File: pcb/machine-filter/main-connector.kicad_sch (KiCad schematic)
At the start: 3 parts

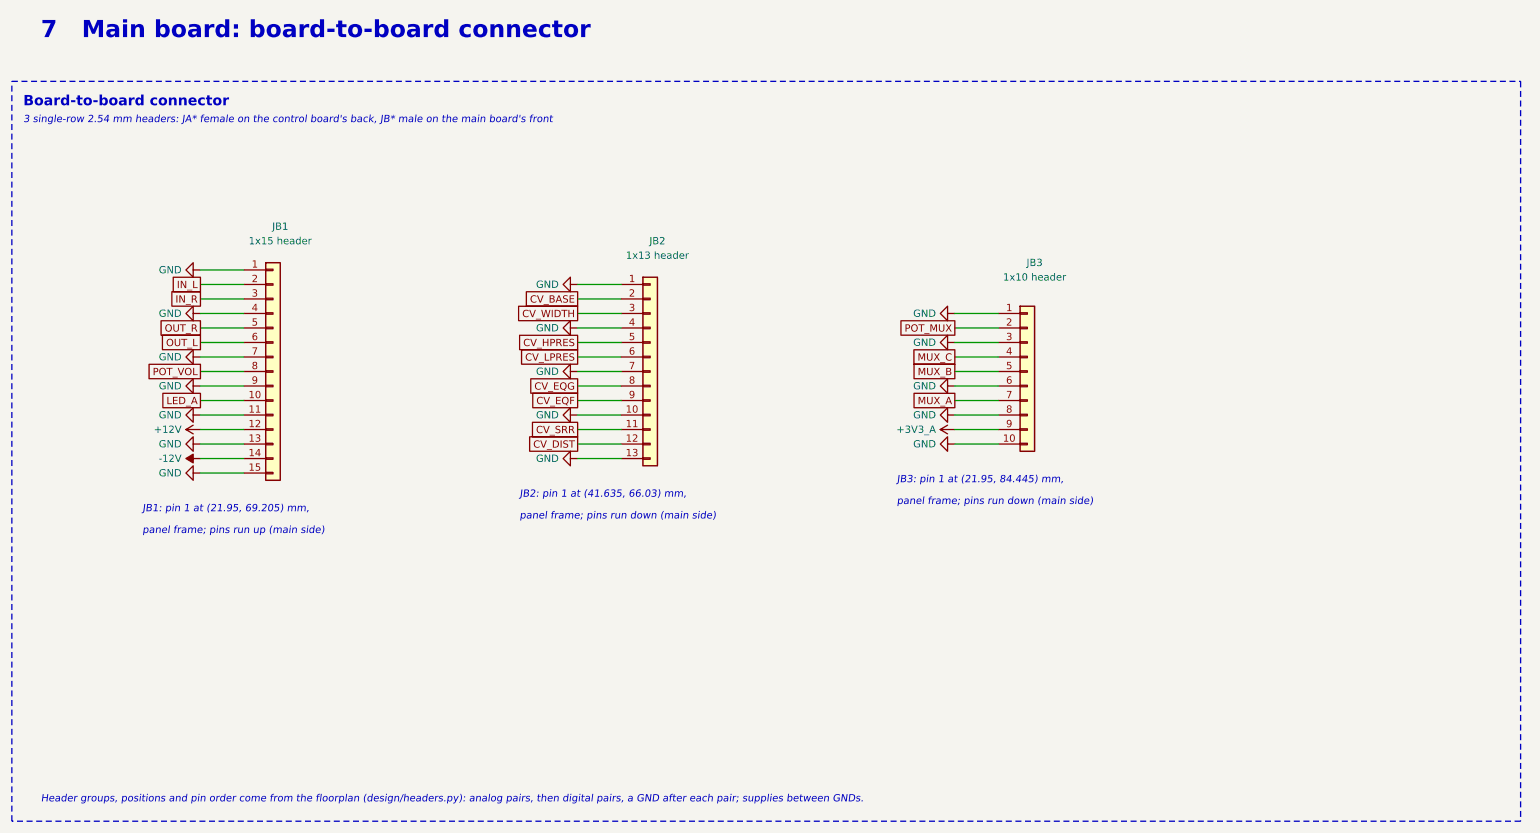
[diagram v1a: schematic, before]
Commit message: Control chips placed; board-to-board connectors found by search: 4 lines (22+3+5+3 pins, 12 ground)
connector_search.py: lines live in legal straight runs on both boards (courtyard polygons, socket body and its
courtyard, leads under bodies), d's ground rules plus a ground on every connector; simulated annealing, 12
restarts. sync_headers.py deletes and re-adds the header footprints from the schematic, places both boards and
checks every pin pair lines up. auto_place.py now keeps other parts' leads out from under a body (U6 had RV4's
lead under it). Mux channels and LED sections re-checked: already shortest. Build OK, raw DRC: no real problems.

Co-Authored-By: Claude Opus 5.5 <noreply@anthropic.com>
Claude-Session: https://claude.ai/code/session_01Cf5qNBi3oNHhbCjPHvswth
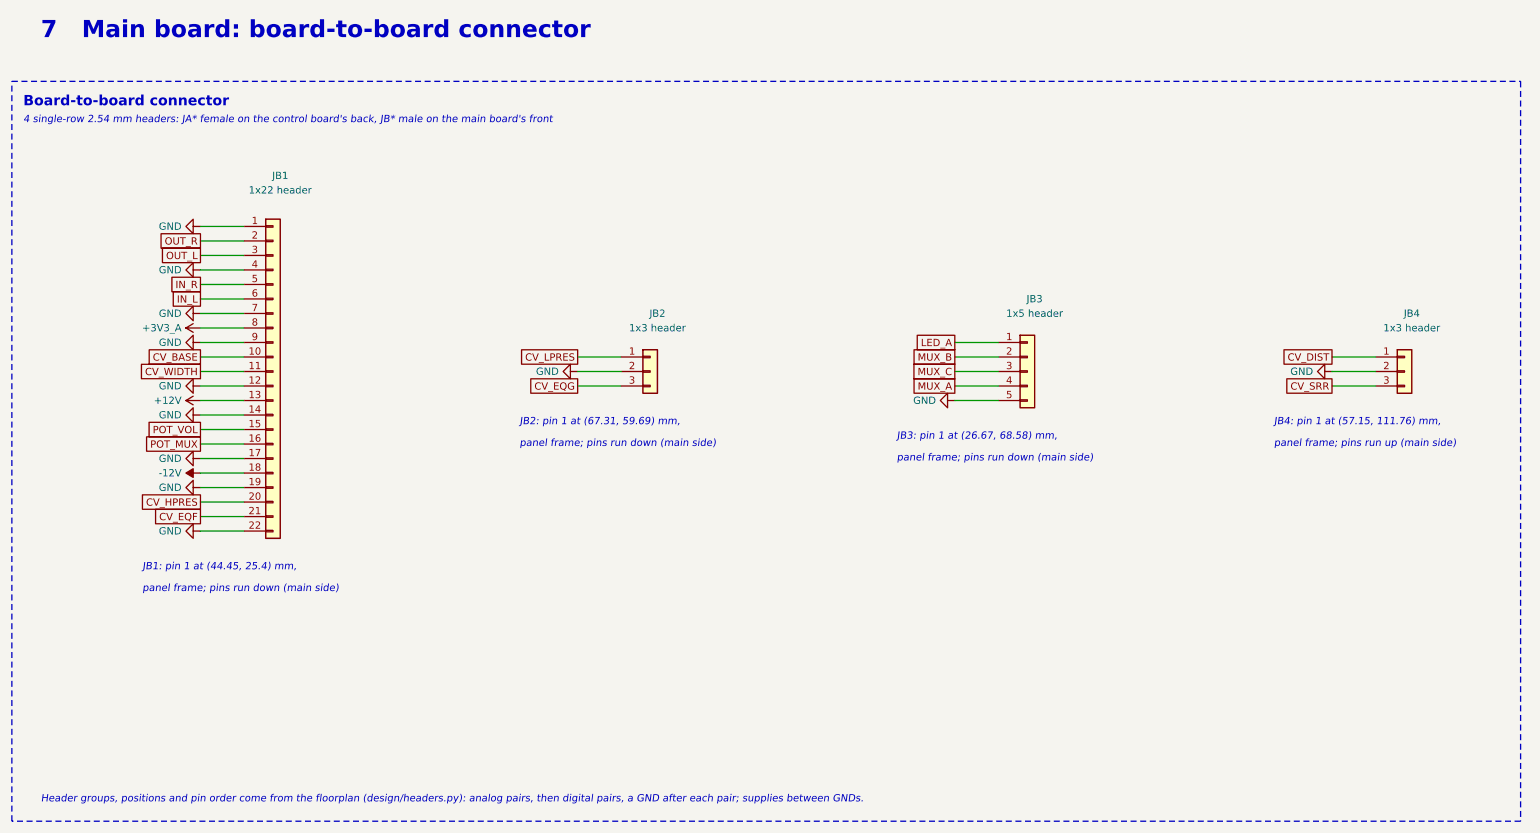
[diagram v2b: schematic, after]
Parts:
- added JB4: 1x3 header, Connector_PinHeader_2.54mm:PinHeader_1x03_P2.54mm_Vertical, symbol Connector_Generic:Conn_01x03
- JB1: value 1x15 header -> 1x22 header; footprint Connector_PinHeader_2.54mm:PinHeader_1x15_P2.54mm_Vertical -> Connector_PinHeader_2.54mm:PinHeader_1x22_P2.54mm_Vertical; symbol Connector_Generic:Conn_01x15 -> Connector_Generic:Conn_01x22; MPN 2.54 mm male pin header 1x15 -> 2.54 mm male pin header 1x22
- JB2: value 1x13 header -> 1x3 header; footprint Connector_PinHeader_2.54mm:PinHeader_1x13_P2.54mm_Vertical -> Connector_PinHeader_2.54mm:PinHeader_1x03_P2.54mm_Vertical; symbol Connector_Generic:Conn_01x13 -> Connector_Generic:Conn_01x03; MPN 2.54 mm male pin header 1x13 -> 2.54 mm male pin header 1x3
- JB3: value 1x10 header -> 1x5 header; footprint Connector_PinHeader_2.54mm:PinHeader_1x10_P2.54mm_Vertical -> Connector_PinHeader_2.54mm:PinHeader_1x05_P2.54mm_Vertical; symbol Connector_Generic:Conn_01x10 -> Connector_Generic:Conn_01x05; MPN 2.54 mm male pin header 1x10 -> 2.54 mm male pin header 1x5
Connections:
- net +12V: now also JB1.13 (Pin_13); no longer JB1.12 (Pin_12)
- net +3V3_A: now also JB1.8 (Pin_8); no longer JB3.9 (Pin_9)
- net -12V: now also JB1.18 (Pin_18); no longer JB1.14 (Pin_14)
- net CV_BASE: now also JB1.10 (Pin_10); no longer JB2.2 (Pin_2)
- net CV_DIST: now also JB4.1 (Pin_1); no longer JB2.12 (Pin_12)
- net CV_EQF: now also JB1.21 (Pin_21); no longer JB2.9 (Pin_9)
- net CV_EQG: now also JB2.3 (Pin_3); no longer JB2.8 (Pin_8)
- net CV_HPRES: now also JB1.20 (Pin_20); no longer JB2.5 (Pin_5)
- net CV_LPRES: now also JB2.1 (Pin_1); no longer JB2.6 (Pin_6)
- net CV_SRR: now also JB4.3 (Pin_3); no longer JB2.11 (Pin_11)
- net CV_WIDTH: now also JB1.11 (Pin_11); no longer JB2.3 (Pin_3)
- net GND: now also JB1.12 (Pin_12), JB1.14 (Pin_14), JB1.17 (Pin_17), JB1.19 (Pin_19), JB1.22 (Pin_22), JB2.2 (Pin_2), JB3.5 (Pin_5), JB4.2 (Pin_2); no longer JB1.11 (Pin_11), JB1.13 (Pin_13), JB1.15 (Pin_15), JB2.1 (Pin_1), JB2.10 (Pin_10), JB2.13 (Pin_13), JB2.4 (Pin_4), JB2.7 (Pin_7), JB3.1 (Pin_1), JB3.10 (Pin_10), JB3.3 (Pin_3), JB3.6 (Pin_6), JB3.8 (Pin_8)
- net IN_L: now also JB1.6 (Pin_6); no longer JB1.2 (Pin_2)
- net IN_R: now also JB1.5 (Pin_5); no longer JB1.3 (Pin_3)
- net LED_A: now also JB3.1 (Pin_1); no longer JB1.10 (Pin_10)
- net MUX_A: now also JB3.4 (Pin_4); no longer JB3.7 (Pin_7)
- net MUX_B: now also JB3.2 (Pin_2); no longer JB3.5 (Pin_5)
- net MUX_C: now also JB3.3 (Pin_3); no longer JB3.4 (Pin_4)
- net OUT_L: now also JB1.3 (Pin_3); no longer JB1.6 (Pin_6)
- net OUT_R: now also JB1.2 (Pin_2); no longer JB1.5 (Pin_5)
- net POT_MUX: now also JB1.16 (Pin_16); no longer JB3.2 (Pin_2)
- net POT_VOL: now also JB1.15 (Pin_15); no longer JB1.8 (Pin_8)
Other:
- note added: "4 single-row 2.54 mm headers: JA* female on the control board's back, JB* male on the main board's front"
- note added: "JB1: pin 1 at (44.45, 25.4) mm,"
- note added: "JB2: pin 1 at (67.31, 59.69) mm,"
- note added: "JB3: pin 1 at (26.67, 68.58) mm,"
- note added: "JB4: pin 1 at (57.15, 111.76) mm,"
- note removed: "3 single-row 2.54 mm headers: JA* female on the control board's back, JB* male on the main board's front"
- note removed: "JB1: pin 1 at (21.95, 69.205) mm,"
- note removed: "JB2: pin 1 at (41.635, 66.03) mm,"
- note removed: "JB3: pin 1 at (21.95, 84.445) mm,"

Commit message: Hand-soldering clearance (d: 1.25 mm): connectors re-searched, control parts re-placed
connector_search.py: header pads keep 1.25 mm from every other pad on both boards and from the whole box around
each jack, pot and LED (taken from the square pin-1 pad); --free leaves parts to be re-placed out of the search.
auto_place.py: control-board through-hole pads and anything near a header keep 1.25 mm; --free re-places parts.
Result: 3 lines, 30 + 5 + 2 pins (16 ground); the connector beside pot RV5 and the one between two CV jacks are
gone. Measured: nearest header-pad gap 1.35 mm, header to a body box 1.31 mm. Raw DRC: no real problems.

Co-Authored-By: Claude Opus 5.5 <noreply@anthropic.com>
Claude-Session: https://claude.ai/code/session_01Cf5qNBi3oNHhbCjPHvswth
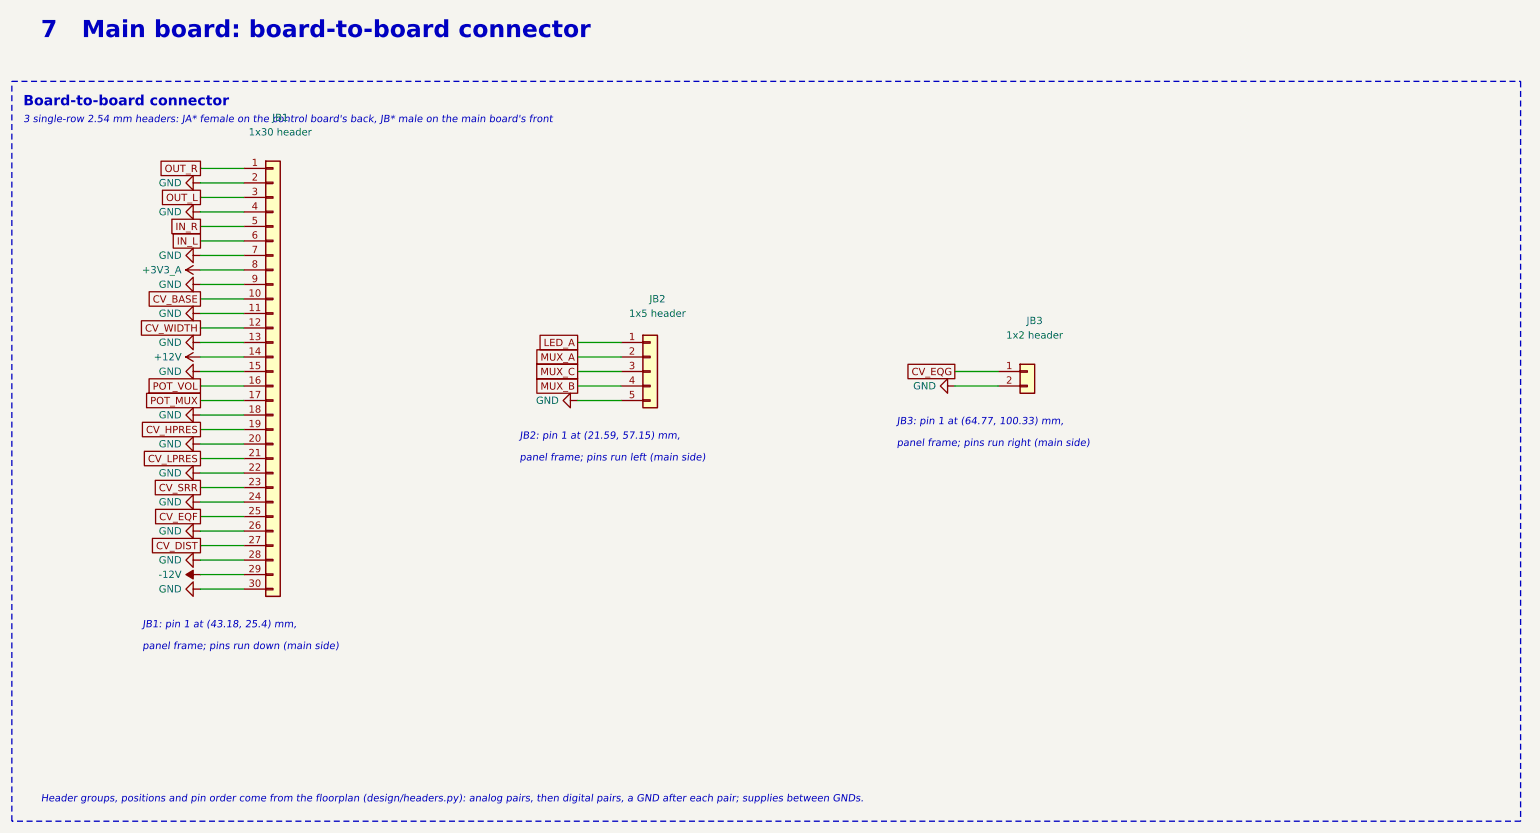
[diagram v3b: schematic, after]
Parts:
- removed JB4: 1x3 header, Connector_PinHeader_2.54mm:PinHeader_1x03_P2.54mm_Vertical, symbol Connector_Generic:Conn_01x03
- JB1: value 1x22 header -> 1x30 header; footprint Connector_PinHeader_2.54mm:PinHeader_1x22_P2.54mm_Vertical -> Connector_PinHeader_2.54mm:PinHeader_1x30_P2.54mm_Vertical; symbol Connector_Generic:Conn_01x22 -> Connector_Generic:Conn_01x30; MPN 2.54 mm male pin header 1x22 -> 2.54 mm male pin header 1x30
- JB2: value 1x3 header -> 1x5 header; footprint Connector_PinHeader_2.54mm:PinHeader_1x03_P2.54mm_Vertical -> Connector_PinHeader_2.54mm:PinHeader_1x05_P2.54mm_Vertical; symbol Connector_Generic:Conn_01x03 -> Connector_Generic:Conn_01x05; MPN 2.54 mm male pin header 1x3 -> 2.54 mm male pin header 1x5
- JB3: value 1x5 header -> 1x2 header; footprint Connector_PinHeader_2.54mm:PinHeader_1x05_P2.54mm_Vertical -> Connector_PinHeader_2.54mm:PinHeader_1x02_P2.54mm_Vertical; symbol Connector_Generic:Conn_01x05 -> Connector_Generic:Conn_01x02; MPN 2.54 mm male pin header 1x5 -> 2.54 mm male pin header 1x2
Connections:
- net +12V: now also JB1.14 (Pin_14); no longer JB1.13 (Pin_13)
- net -12V: now also JB1.29 (Pin_29); no longer JB1.18 (Pin_18)
- net CV_DIST: now also JB1.27 (Pin_27)
- net CV_EQF: now also JB1.25 (Pin_25); no longer JB1.21 (Pin_21)
- net CV_EQG: now also JB3.1 (Pin_1); no longer JB2.3 (Pin_3)
- net CV_HPRES: now also JB1.19 (Pin_19); no longer JB1.20 (Pin_20)
- net CV_LPRES: now also JB1.21 (Pin_21); no longer JB2.1 (Pin_1)
- net CV_SRR: now also JB1.23 (Pin_23)
- net CV_WIDTH: now also JB1.12 (Pin_12); no longer JB1.11 (Pin_11)
- net GND: now also JB1.11 (Pin_11), JB1.13 (Pin_13), JB1.15 (Pin_15), JB1.18 (Pin_18), JB1.2 (Pin_2), JB1.20 (Pin_20), JB1.24 (Pin_24), JB1.26 (Pin_26), JB1.28 (Pin_28), JB1.30 (Pin_30), JB2.5 (Pin_5), JB3.2 (Pin_2); no longer JB1.1 (Pin_1), JB1.12 (Pin_12), JB1.14 (Pin_14), JB1.17 (Pin_17), JB1.19 (Pin_19), JB2.2 (Pin_2), JB3.5 (Pin_5)
- net LED_A: now also JB2.1 (Pin_1); no longer JB3.1 (Pin_1)
- net MUX_A: now also JB2.2 (Pin_2); no longer JB3.4 (Pin_4)
- net MUX_B: now also JB2.4 (Pin_4); no longer JB3.2 (Pin_2)
- net MUX_C: now also JB2.3 (Pin_3); no longer JB3.3 (Pin_3)
- net OUT_R: now also JB1.1 (Pin_1); no longer JB1.2 (Pin_2)
- net POT_MUX: now also JB1.17 (Pin_17); no longer JB1.16 (Pin_16)
- net POT_VOL: now also JB1.16 (Pin_16); no longer JB1.15 (Pin_15)
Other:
- note added: "3 single-row 2.54 mm headers: JA* female on the control board's back, JB* male on the main board's front"
- note added: "JB1: pin 1 at (43.18, 25.4) mm,"
- note added: "JB2: pin 1 at (21.59, 57.15) mm,"
- note added: "JB3: pin 1 at (64.77, 100.33) mm,"
- note added: "panel frame; pins run left (main side)"
- note added: "panel frame; pins run right (main side)"
- note removed: "4 single-row 2.54 mm headers: JA* female on the control board's back, JB* male on the main board's front"
- note removed: "JB1: pin 1 at (44.45, 25.4) mm,"
- note removed: "JB2: pin 1 at (67.31, 59.69) mm,"
- note removed: "JB3: pin 1 at (26.67, 68.58) mm,"
- note removed: "JB4: pin 1 at (57.15, 111.76) mm,"
- note removed: "panel frame; pins run up (main side)"

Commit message: Experiment (not chosen): connectors searched with a strict Seed-pocket rule; routing tool runs
The board now holds the pocket-rule connectors (4 lines, 34 pins) as an experiment; c08-handsolder (3 lines,
routed: main 5 unrouted / 61 vias, control 2 unrouted / 16 vias, DRC 0) stays the best candidate. route_board.py:
Freerouting 2.3 ignores direction costs from DSN, CLI and freerouting.json (tested); 90-degree snap works.
Paused for d: the header loop is repeating (post-mortem 2026-10-06).

Co-Authored-By: Claude Opus 5.5 <noreply@anthropic.com>
Claude-Session: https://claude.ai/code/session_01Cf5qNBi3oNHhbCjPHvswth
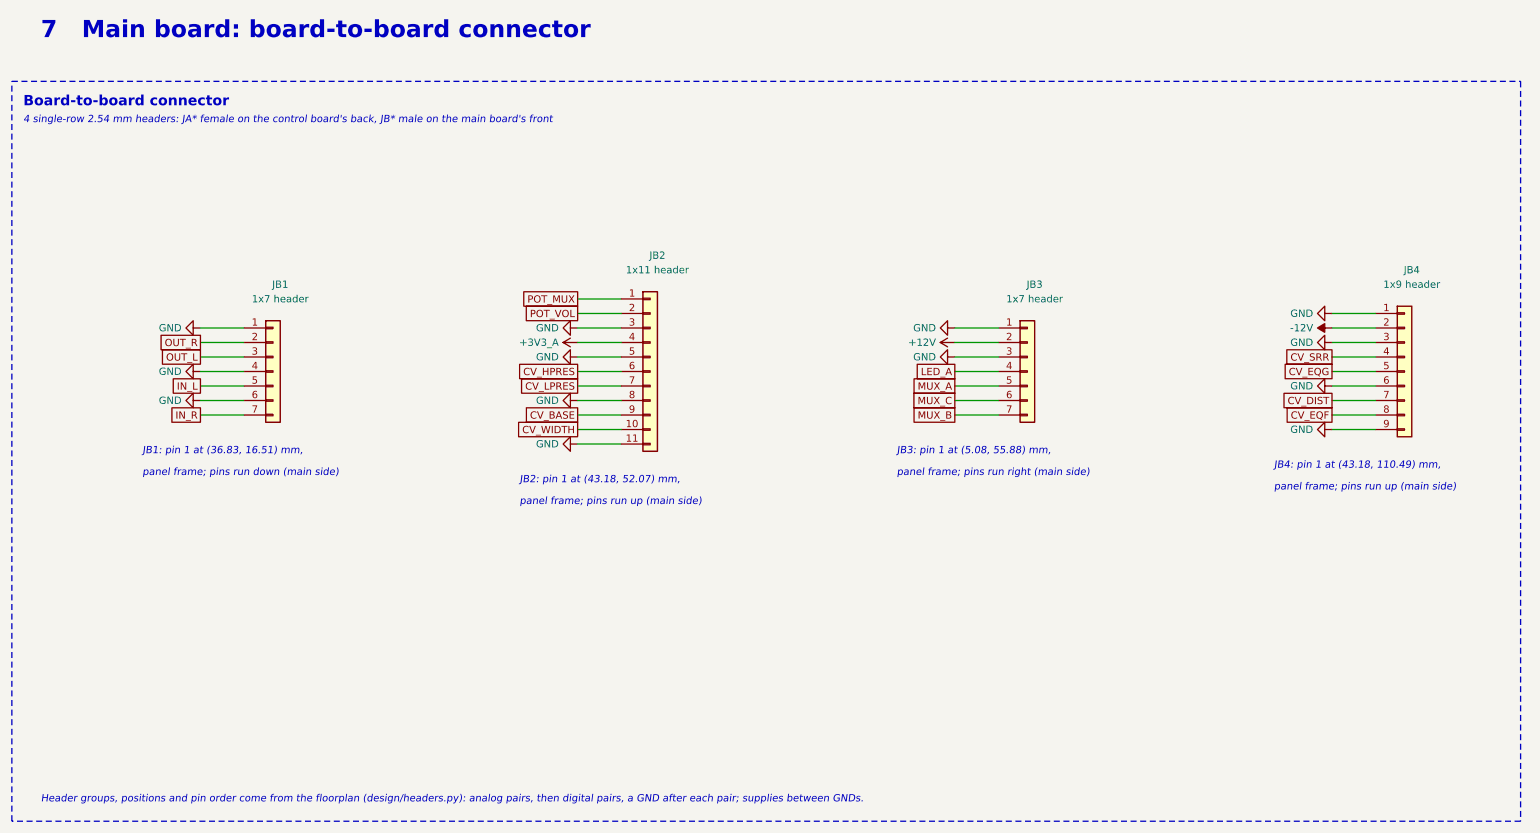
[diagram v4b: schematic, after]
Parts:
- added JB4: 1x9 header, Connector_PinHeader_2.54mm:PinHeader_1x09_P2.54mm_Vertical, symbol Connector_Generic:Conn_01x09
- JB1: value 1x30 header -> 1x7 header; footprint Connector_PinHeader_2.54mm:PinHeader_1x30_P2.54mm_Vertical -> Connector_PinHeader_2.54mm:PinHeader_1x07_P2.54mm_Vertical; symbol Connector_Generic:Conn_01x30 -> Connector_Generic:Conn_01x07; MPN 2.54 mm male pin header 1x30 -> 2.54 mm male pin header 1x7
- JB2: value 1x5 header -> 1x11 header; footprint Connector_PinHeader_2.54mm:PinHeader_1x05_P2.54mm_Vertical -> Connector_PinHeader_2.54mm:PinHeader_1x11_P2.54mm_Vertical; symbol Connector_Generic:Conn_01x05 -> Connector_Generic:Conn_01x11; MPN 2.54 mm male pin header 1x5 -> 2.54 mm male pin header 1x11
- JB3: value 1x2 header -> 1x7 header; footprint Connector_PinHeader_2.54mm:PinHeader_1x02_P2.54mm_Vertical -> Connector_PinHeader_2.54mm:PinHeader_1x07_P2.54mm_Vertical; symbol Connector_Generic:Conn_01x02 -> Connector_Generic:Conn_01x07; MPN 2.54 mm male pin header 1x2 -> 2.54 mm male pin header 1x7
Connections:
- net +12V: now also JB3.2 (Pin_2); no longer JB1.14 (Pin_14)
- net +3V3_A: now also JB2.4 (Pin_4); no longer JB1.8 (Pin_8)
- net -12V: now also JB4.2 (Pin_2); no longer JB1.29 (Pin_29)
- net CV_BASE: now also JB2.9 (Pin_9); no longer JB1.10 (Pin_10)
- net CV_DIST: now also JB4.7 (Pin_7); no longer JB1.27 (Pin_27)
- net CV_EQF: now also JB4.8 (Pin_8); no longer JB1.25 (Pin_25)
- net CV_EQG: now also JB4.5 (Pin_5); no longer JB3.1 (Pin_1)
- net CV_HPRES: now also JB2.6 (Pin_6); no longer JB1.19 (Pin_19)
- net CV_LPRES: now also JB2.7 (Pin_7); no longer JB1.21 (Pin_21)
- net CV_SRR: now also JB4.4 (Pin_4); no longer JB1.23 (Pin_23)
- net CV_WIDTH: now also JB2.10 (Pin_10); no longer JB1.12 (Pin_12)
- net GND: now also JB1.1 (Pin_1), JB1.6 (Pin_6), JB2.11 (Pin_11), JB2.3 (Pin_3), JB2.8 (Pin_8), JB3.1 (Pin_1), JB3.3 (Pin_3), JB4.1 (Pin_1), JB4.3 (Pin_3), JB4.6 (Pin_6), JB4.9 (Pin_9); no longer JB1.11 (Pin_11), JB1.13 (Pin_13), JB1.15 (Pin_15), JB1.18 (Pin_18), JB1.2 (Pin_2), JB1.20 (Pin_20), JB1.22 (Pin_22), JB1.24 (Pin_24), JB1.26 (Pin_26), JB1.28 (Pin_28), JB1.30 (Pin_30), JB1.7 (Pin_7), JB1.9 (Pin_9), JB3.2 (Pin_2)
- net IN_L: now also JB1.5 (Pin_5); no longer JB1.6 (Pin_6)
- net IN_R: now also JB1.7 (Pin_7); no longer JB1.5 (Pin_5)
- net LED_A: now also JB3.4 (Pin_4); no longer JB2.1 (Pin_1)
- net MUX_A: now also JB3.5 (Pin_5); no longer JB2.2 (Pin_2)
- net MUX_B: now also JB3.7 (Pin_7); no longer JB2.4 (Pin_4)
- net MUX_C: now also JB3.6 (Pin_6); no longer JB2.3 (Pin_3)
- net OUT_R: now also JB1.2 (Pin_2); no longer JB1.1 (Pin_1)
- net POT_MUX: now also JB2.1 (Pin_1); no longer JB1.17 (Pin_17)
- net POT_VOL: now also JB2.2 (Pin_2); no longer JB1.16 (Pin_16)
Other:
- note added: "4 single-row 2.54 mm headers: JA* female on the control board's back, JB* male on the main board's front"
- note added: "JB1: pin 1 at (36.83, 16.51) mm,"
- note added: "JB2: pin 1 at (43.18, 52.07) mm,"
- note added: "JB3: pin 1 at (5.08, 55.88) mm,"
- note added: "JB4: pin 1 at (43.18, 110.49) mm,"
- note added: "panel frame; pins run up (main side)"
- note removed: "3 single-row 2.54 mm headers: JA* female on the control board's back, JB* male on the main board's front"
- note removed: "JB1: pin 1 at (43.18, 25.4) mm,"
- note removed: "JB2: pin 1 at (21.59, 57.15) mm,"
- note removed: "JB3: pin 1 at (64.77, 100.33) mm,"
- note removed: "panel frame; pins run left (main side)"
